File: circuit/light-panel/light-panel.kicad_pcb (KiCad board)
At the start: 2 copper layers, 32 parts, among them J1 Screw_Terminal_01x02

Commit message: Draw layout
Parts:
- removed the R2 at (129.7, 85.0)
- removed the R3 at (129.7, 87.5)
- moved C1 53.3 mm to (93.0, 109.5)
- moved J1 52.8 mm to (90.3, 98.0), turned to -90 degrees
- moved R3 43.6 mm to (99.0, 112.0)
- moved R2 41.1 mm to (99.0, 100.0)
- moved D7 37.6 mm to (109.0, 108.0), turned to 180 degrees
- moved R1 36.9 mm to (99.0, 103.0)
- moved D12 35.7 mm to (114.0, 108.0)
- moved D8 35.5 mm to (109.0, 104.0)
- moved D14 35.3 mm to (114.0, 112.0)
- moved D11 35.3 mm to (114.0, 104.0)
- moved D9 34.6 mm to (109.0, 100.0), turned to 180 degrees
- moved R4 34.1 mm to (105.5, 96.0), turned to -90 degrees
- moved D16 33.6 mm to (119.0, 104.0)
- moved D18 33.4 mm to (119.0, 108.0)
- moved D15 33.3 mm to (119.0, 100.0)
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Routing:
- net +5V: track 0.00 -> 101.1 mm
- net Net-(D11-A): track 0.00 -> 13.6 mm
- net Net-(D7-A): track 0.00 -> 12.3 mm
- net Net-(D5-K): track 0.00 -> 5.83 mm
- net Net-(D1-K): track 0.00 -> 5.83 mm
- net Net-(D15-K): track 0.00 -> 4.65 mm
- net Net-(D11-K): track 0.00 -> 4.65 mm
- net Net-(D17-K): track 0.00 -> 4.25 mm
- net Net-(D3-K): track 0.00 -> 4.21 mm
- net Net-(D17-A): track 0.00 -> 4.17 mm
- net Net-(D7-K): track 0.00 -> 4.00 mm
- net Net-(D15-A): track 0.00 -> 3.59 mm
- net Net-(D13-K): track 0.00 -> 3.43 mm
- net Net-(D10-A): track 0.00 -> 3.43 mm
- net Net-(D5-A): track 0.00 -> 3.39 mm
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- added copper zone on F.Cu, net GND
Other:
- board outline added: 45 x 20 mm

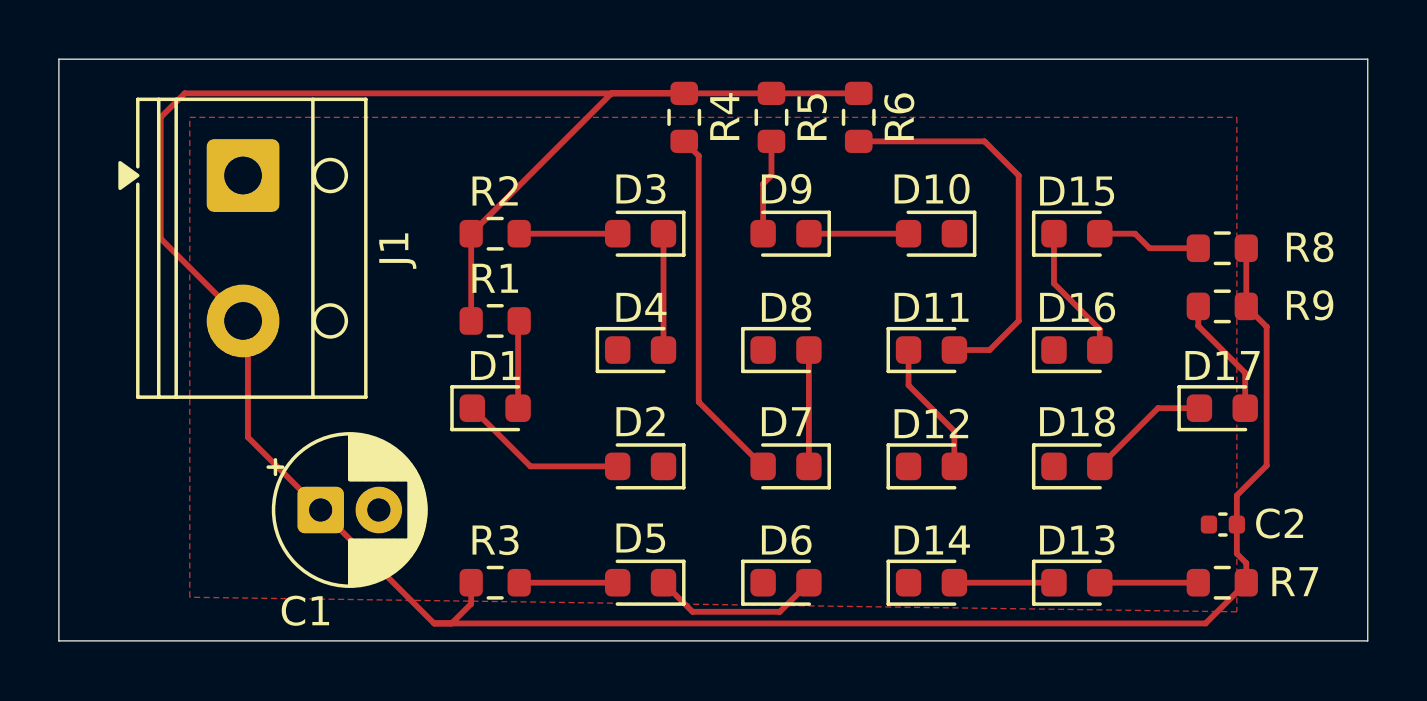
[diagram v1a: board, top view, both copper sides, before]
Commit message: Add holding screw
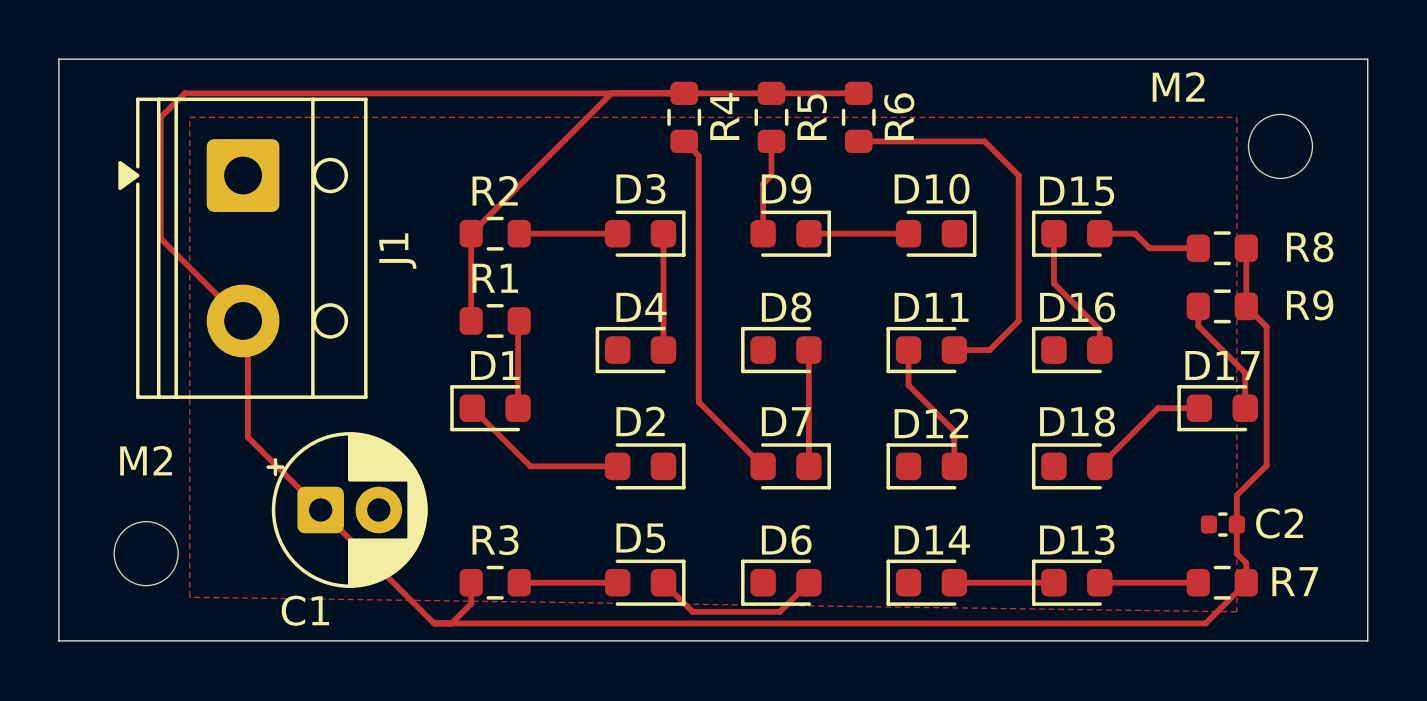
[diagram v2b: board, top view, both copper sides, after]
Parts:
- added M2: MountingHole, MountingHole:MountingHole_2.2mm_M2, F.Cu at (126.0, 97.0)
- added M2: MountingHole, MountingHole:MountingHole_2.2mm_M2, F.Cu at (87.0, 111.0)
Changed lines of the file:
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@@
 		)
+	)
+	(footprint "MountingHole:MountingHole_2.2mm_M2"
+		(layer "F.Cu")
+		(at 126 97)
+		(descr "Mounting Hole 2.2mm, M2, no annular, generated by kicad-footprint-generator mountinghole.py")
+		(tags "mountinghole M2")
+		(property "Reference" "M2"
+			(at -3.5 -2 0)
+			(layer "F.SilkS")
+			(effects
+				(font
+					(size 1 1)
+					(thickness 0.15)
+				)
+			)
+		)
+		(property "Value" "MountingHole"
+			(at 0 3.15 0)
+			(layer "F.Fab")
+			(effects
+				(font
+					(size 1 1)
+					(thickness 0.15)
+				)
+			)
+		)
+		(property "Datasheet" ""
+			(at 0 0 0)
+			(layer "F.Fab")
+			(hide yes)
+			(effects
+				(font
+					(size 1.27 1.27)
+				)
+			)
+		)
+		(property "Description" "Mounting Hole without connection"
+			(at 0 0 0)
+			(layer "F.Fab")
+			(hide yes)
+			(effects
+				(font
+					(size 1.27 1.27)
+				)
+			)
+		)
+		(property "KiLib_Generator" "mounting_hardware/mounting_hole"
+			(at 0 0 0)
+			(layer "F.SilkS")
+			(hide yes)
+			(effects
+				(font
+					(size 1 1)
+					(thickness 0.15)
+				)
+			)
+		)
+		(property ki_fp_filters "MountingHole*")
+		(sheetname "/")
+		(sheetfile "light-panel.kicad_sch")
+		(units
+			(unit
+				(name "A")
+				(pins)
+			)
+		)
+		(attr exclude_from_bom)
+		(duplicate_pad_numbers_are_jumpers no)
+		(fp_circle
+			(center 0 0)
+			(end 2.2 0)
+			(stroke
+				(width 0.15)
+				(type solid)
+			)
+			(fill no)
+			(layer "Cmts.User")
+		)
+		(fp_circle
+			(center 0 0)
+			(end 2.45 0)
+			(stroke
+				(width 0.05)
+				(type solid)
+			)
+			(fill no)
+			(layer "F.CrtYd")
+		)
+		(fp_text user "${REFERENCE}"
+			(at 0 0 0)
+			(layer "F.Fab")
+			(effects
+				(font
+					(size 1 1)
+					(thickness 0.15)
+				)
+			)
+		)
+		(pad "" np_thru_hole circle
+			(at 0 0)
+			(size 2.2 2.2)
+			(drill 2.2)
+			(layers "*.Cu" "*.Mask")
+		)
+		(embedded_fonts no)
+	)
+	(footprint "MountingHole:MountingHole_2.2mm_M2"
+		(layer "F.Cu")
+		(at 87 111)
+		(descr "Mounting Hole 2.2mm, M2, no annular, generated by kicad-footprint-generator mountinghole.py")
+		(tags "mountinghole M2")
+		(property "Reference" "M2"
+			(at 0 -3.15 0)
+			(layer "F.SilkS")
+			(effects
+				(font
+					(size 1 1)
+					(thickness 0.15)
+				)
+			)
+		)
+		(property "Value" "MountingHole"
+			(at 0 3.15 0)
+			(layer "F.Fab")
+			(effects
+				(font
+					(size 1 1)
+					(thickness 0.15)
+				)
+			)
+		)
+		(property "Datasheet" ""
+			(at 0 0 0)
+			(layer "F.Fab")
+			(hide yes)
+			(effects
+				(font
+					(size 1.27 1.27)
+				)
+			)
+		)
+		(property "Description" "Mounting Hole without connection"
+			(at 0 0 0)
+			(layer "F.Fab")
+			(hide yes)
+			(effects
+				(font
+					(size 1.27 1.27)
+				)
+			)
+		)
+		(property "KiLib_Generator" "mounting_hardware/mounting_hole"
+			(at 0 0 0)
+			(layer "F.SilkS")
+			(hide yes)
+			(effects
+				(font
+					(size 1 1)
+					(thickness 0.15)
+				)
+			)
+		)
+		(property ki_fp_filters "MountingHole*")
+		(sheetname "/")
+		(sheetfile "light-panel.kicad_sch")
+		(units
+			(unit
+				(name "A")
+				(pins)
+			)
+		)
+		(attr exclude_from_bom)
+		(duplicate_pad_numbers_are_jumpers no)
+		(fp_circle
+			(center 0 0)
+			(end 2.2 0)
+			(stroke
+				(width 0.15)
+				(type solid)
+			)
+			(fill no)
+			(layer "Cmts.User")
+		)
+		(fp_circle
+			(center 0 0)
+			(end 2.45 0)
+			(stroke
+				(width 0.05)
+				(type solid)
+			)
+			(fill no)
+			(layer "F.CrtYd")
+		)
+		(fp_text user "${REFERENCE}"
+			(at 0 0 0)
+			(layer "F.Fab")
+			(effects
+				(font
+					(size 1 1)
+					(thickness 0.15)
+				)
+			)
+		)
+		(pad "" np_thru_hole circle
+			(at 0 0)
+			(size 2.2 2.2)
+			(drill 2.2)
+			(layers "*.Cu" "*.Mask")
+		)
+		(embedded_fonts no)
 	)
 	(footprint "LED_SMD:LED_0603_1608Metric"
